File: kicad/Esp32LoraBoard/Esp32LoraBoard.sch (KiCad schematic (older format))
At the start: 49 parts, among them J1 USB_B_Micro, J2 Power-Selector, J3 Testpoints, J4 ESP_PROG_JTAG, J5 Prog, J6 ext_Measure, J7 Measurement-Selector, J8 OLED_128x64, Q1 UMH3N, Q2 Si2302DS_NMOS, Q3 Si2301DS_PMOS, Q4 Si2302DS_NMOS, Q5 Si2301DS_PMOS, Q6 Si2302DS_NMOS, SW1 Rotary_Encoder, SW2 Reset, U1 LM3940IMP-3.3, U2 ESP32-WROOM-32, U3 RFM95W-868S2

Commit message: Reset Circuit modified. C5 = 100nF now in order to enter programming mode after reset
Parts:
- C5: value 1n -> 100n
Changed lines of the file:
@@
 P 5950 2850
 F 0 "C5" H 5800 2950 50  0000 L CNN
-F 1 "1n" H 5800 2750 50  0000 L CNN
+F 1 "100n" H 5700 2750 50  0000 L CNN
 F 2 "Capacitor_SMD:C_1206_3216Metric_Pad1.42x1.75mm_HandSolder" H 5950 2850 50  0001 C CNN
 F 3 "~" H 5950 2850 50  0001 C CNN

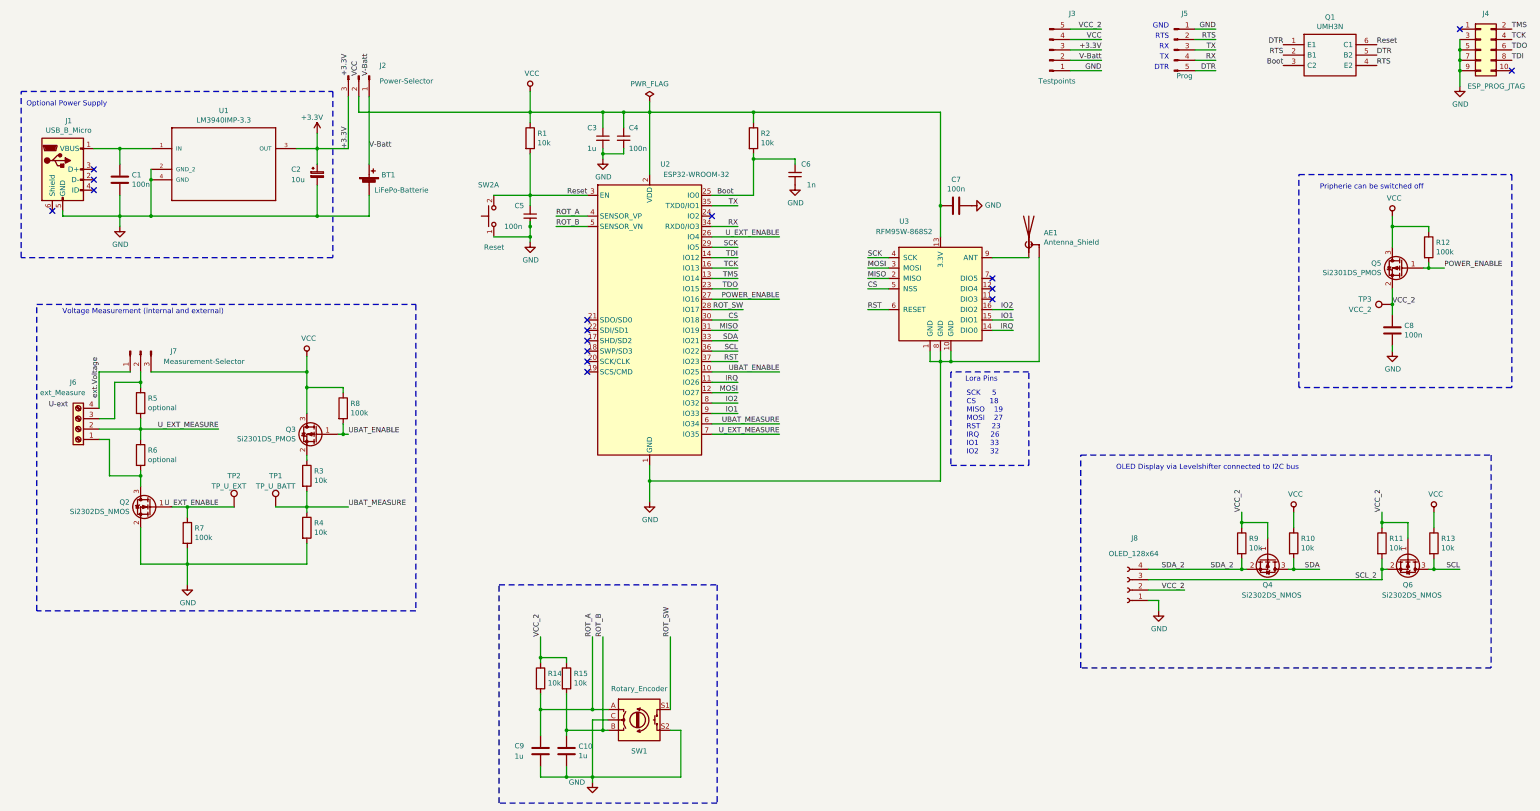
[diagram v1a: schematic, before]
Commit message: exchanged RX/TX and Boot/Reset wires
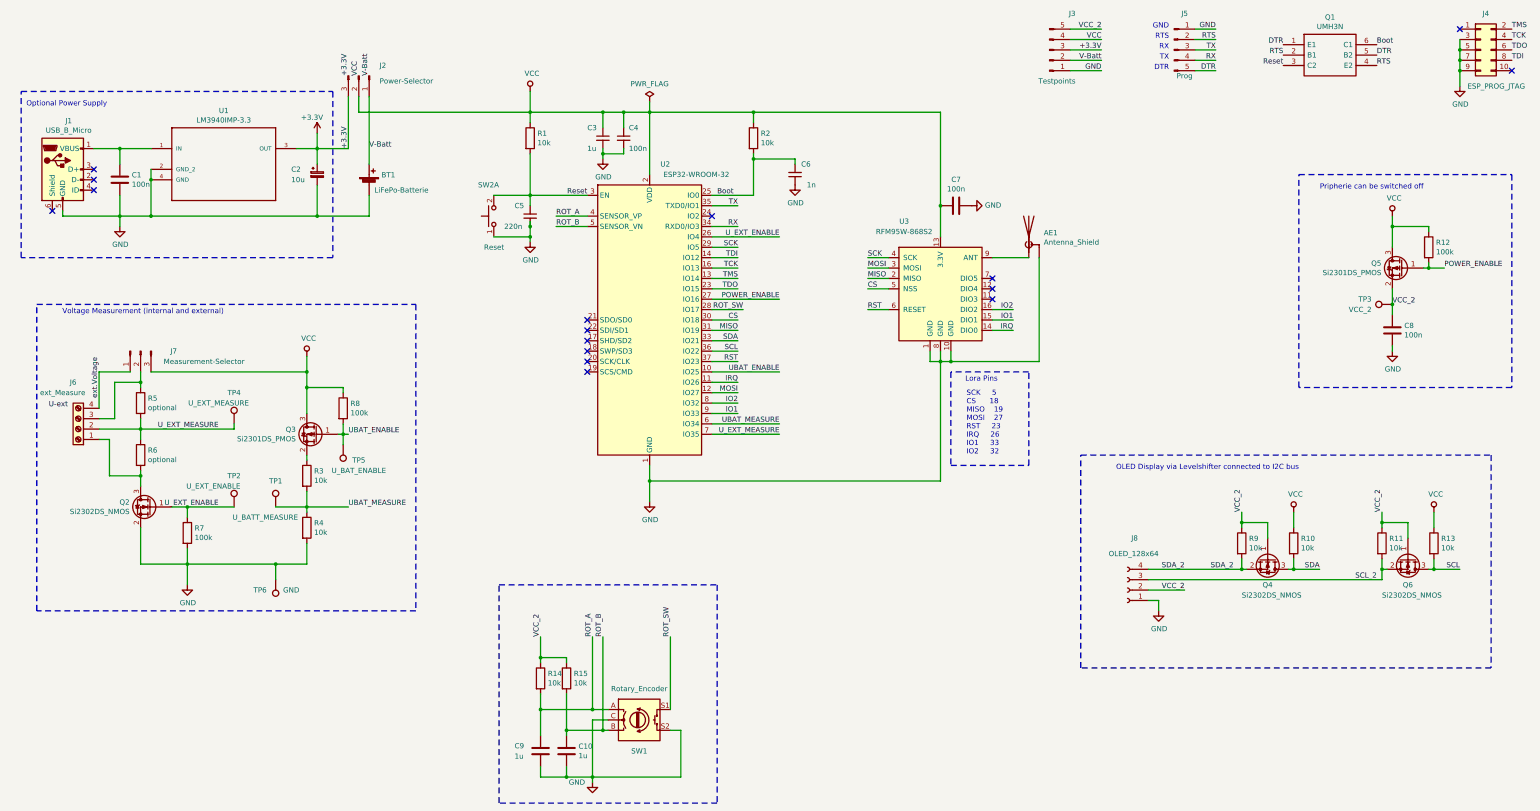
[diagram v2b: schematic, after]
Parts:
- added TP4: U_EXT_MEASURE, Connector_PinHeader_2.54mm:PinHeader_1x01_P2.54mm_Vertical, symbol Connector:TestPoint
- added TP5: U_BAT_ENABLE, Connector_PinHeader_2.54mm:PinHeader_1x01_P2.54mm_Vertical, symbol Connector:TestPoint
- added TP6: GND, Connector_PinHeader_2.54mm:PinHeader_1x01_P2.54mm_Vertical, symbol Connector:TestPoint
- C5: value 100n -> 220n
- TP1: value TP_U_BATT -> U_BATT_MEASURE
- TP2: value TP_U_EXT -> U_EXT_ENABLE
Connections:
- net Boot: now also Q1.6 (C1); no longer Q1.3 (C2)
- net GND: now also TP6.1
- net Reset: now also Q1.3 (C2); no longer Q1.6 (C1)
- net UBAT_ENABLE: now also TP5.1
- net U_EXT_MEASURE: now also TP4.1
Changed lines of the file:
@@
 P 5950 2850
 F 0 "C5" H 5800 2950 50  0000 L CNN
-F 1 "100n" H 5700 2750 50  0000 L CNN
+F 1 "220n" H 5700 2750 50  0000 L CNN
 F 2 "Capacitor_SMD:C_1206_3216Metric_Pad1.42x1.75mm_HandSolder" H 5950 2850 50  0001 C CNN
 F 3 "~" H 5950 2850 50  0001 C CNN
@@
 $EndComp
 Text Label 14100 1200 0    50   ~ 0
-Reset
+Boot
 Text Label 14100 1300 0    50   ~ 0
 DTR
@@
 RTS
 Text Label 13200 1400 2    50   ~ 0
-Boot
+Reset
 $Comp
 L Device:R R2
@@
 Connection ~ 2650 5650
 Wire Wire Line
-	2200 4900 2950 4900
-Wire Wire Line
 	1800 4350 2100 4350
 Wire Wire Line
@@
 U 1 1 5E8ABFC1
 P 3500 5650
-F 0 "TP1" H 3500 5950 50  0000 C CNN
-F 1 "TP_U_BATT" H 3500 5850 50  0000 C CNN
+F 0 "TP1" H 3500 5900 50  0000 C CNN
+F 1 "U_BATT_MEASURE" H 3400 5550 50  0000 C CNN
 F 2 "Connector_PinHeader_2.54mm:PinHeader_1x01_P2.54mm_Vertical" H 3700 5650 50  0001 C CNN
 F 3 "~" H 3700 5650 50  0001 C CNN
@@
 	3800 4200 3800 4350
 Wire Wire Line
-	2650 6200 3800 6200
+	2650 6200 3500 6200
 Wire Wire Line
 	2300 4350 3800 4350
@@
 P 3100 5650
 F 0 "TP2" H 3100 5950 50  0000 C CNN
-F 1 "TP_U_EXT" H 3050 5850 50  0000 C CNN
+F 1 "U_EXT_ENABLE" H 2900 5850 50  0000 C CNN
 F 2 "Connector_PinHeader_2.54mm:PinHeader_1x01_P2.54mm_Vertical" H 3300 5650 50  0001 C CNN
 F 3 "~" H 3300 5650 50  0001 C CNN
@@
 	1    0    0    -1
 $EndComp
+$Comp
+L Connector:TestPoint TP4
+U 1 1 5EA46AF4
+P 3100 4850
+F 0 "TP4" H 3100 5150 50  0000 C CNN
+F 1 "U_EXT_MEASURE" H 2950 5050 50  0000 C CNN
+F 2 "Connector_PinHeader_2.54mm:PinHeader_1x01_P2.54mm_Vertical" H 3300 4850 50  0001 C CNN
+F 3 "~" H 3300 4850 50  0001 C CNN
+	1    3100 4850
+	1    0    0    -1
+$EndComp
+$Comp
+L Connector:TestPoint TP5
+U 1 1 5EA53C46
+P 4150 5050
+F 0 "TP5" H 4000 5200 50  0000 C CNN
+F 1 "U_BAT_ENABLE" H 4000 5300 50  0000 C CNN
+F 2 "Connector_PinHeader_2.54mm:PinHeader_1x01_P2.54mm_Vertical" H 4350 5050 50  0001 C CNN
+F 3 "~" H 4350 5050 50  0001 C CNN
+	1    4150 5050
+	-1   0    0    1
+$EndComp
+Wire Wire Line
+	3100 4900 3100 4850
+Wire Wire Line
+	2200 4900 3100 4900
+Wire Wire Line
+	4150 4950 4150 5050
+$Comp
+L Connector:TestPoint TP6
+U 1 1 5EA89641
+P 3500 6350
+F 0 "TP6" H 3650 6450 50  0000 C CNN
+F 1 "GND" H 3350 6450 50  0000 C CNN
+F 2 "Connector_PinHeader_2.54mm:PinHeader_1x01_P2.54mm_Vertical" H 3700 6350 50  0001 C CNN
+F 3 "~" H 3700 6350 50  0001 C CNN
+	1    3500 6350
+	-1   0    0    1
+$EndComp
+Wire Wire Line
+	3500 6350 3500 6200
+Connection ~ 3500 6200
+Wire Wire Line
+	3500 6200 3800 6200
 $EndSCHEMATC
